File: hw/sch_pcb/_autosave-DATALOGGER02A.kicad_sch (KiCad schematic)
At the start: 9 parts

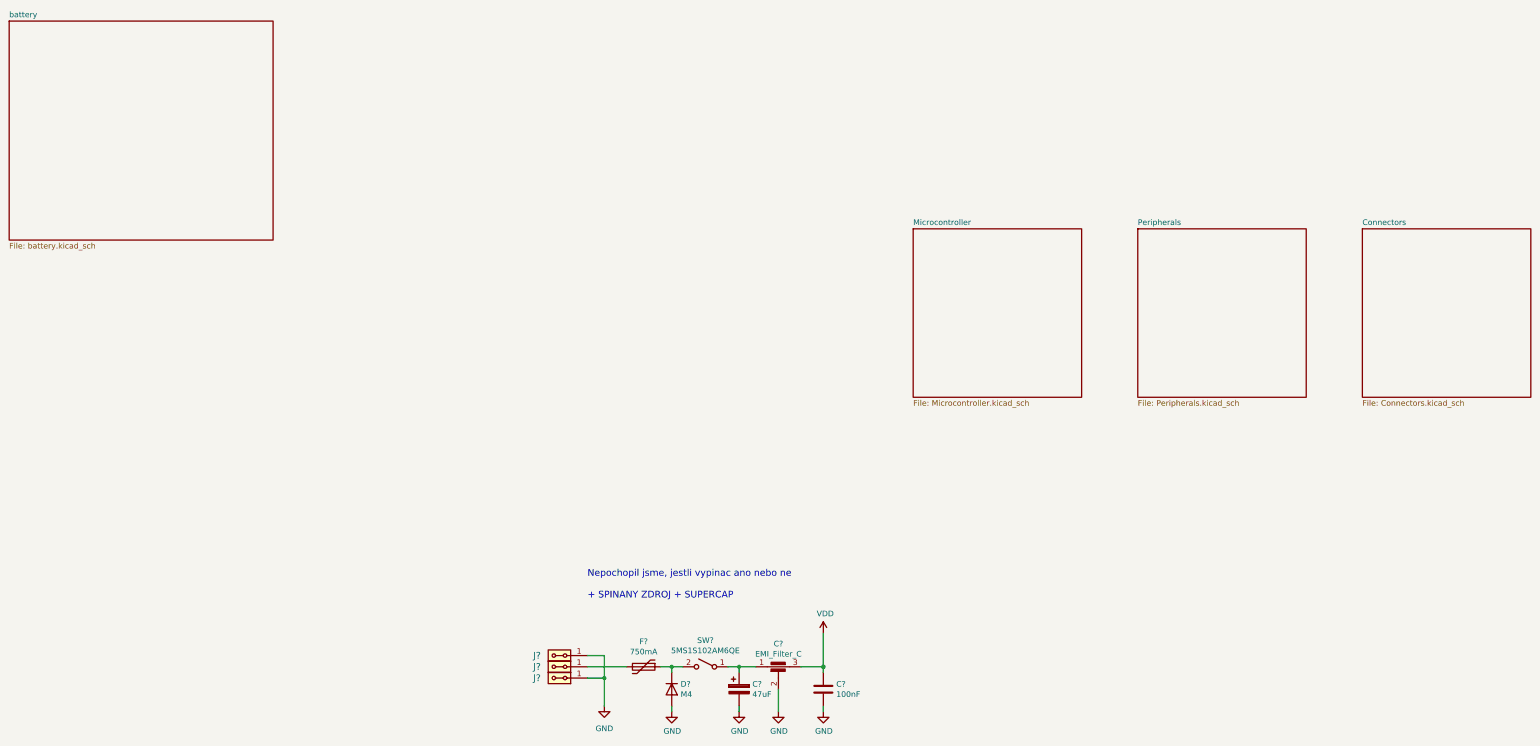
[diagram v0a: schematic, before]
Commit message: update of schematics
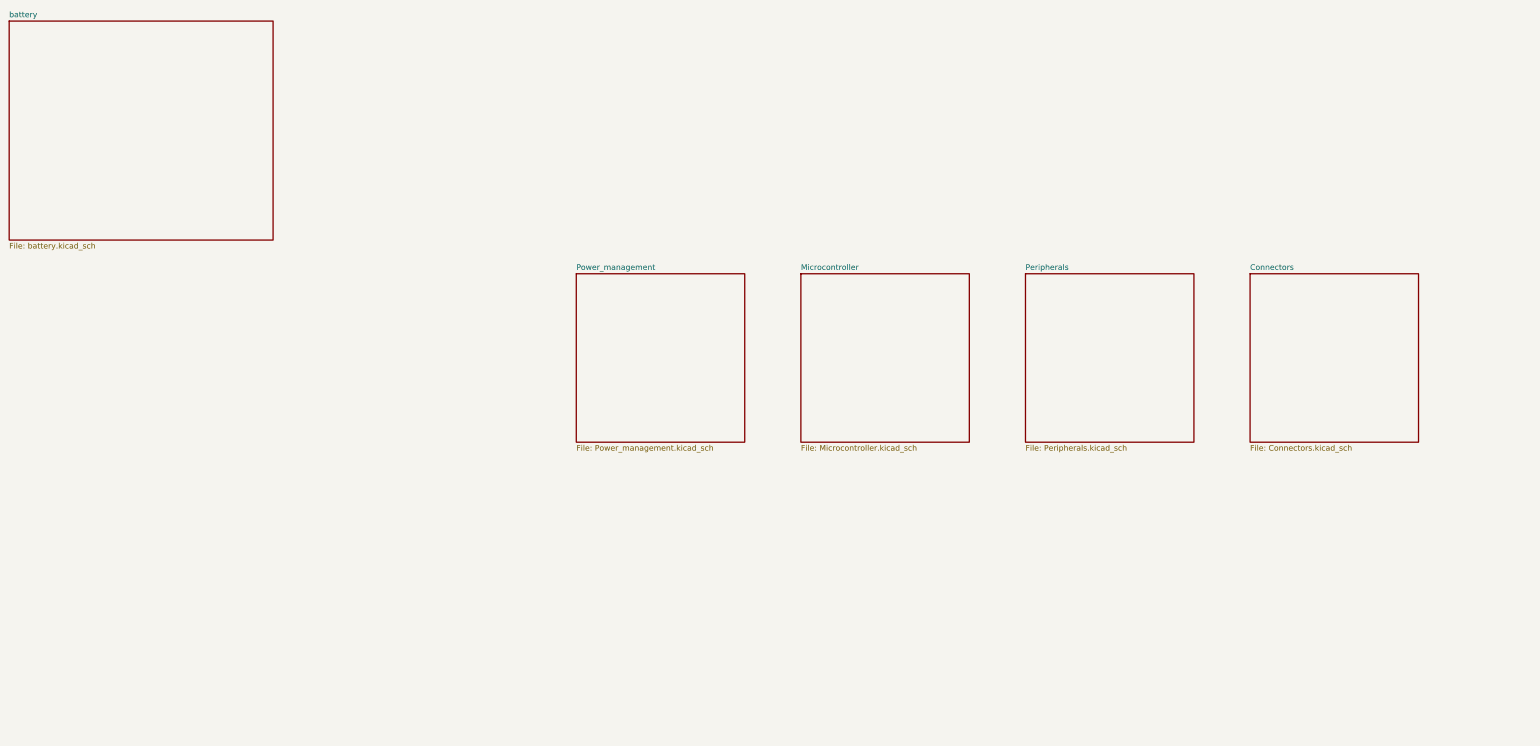
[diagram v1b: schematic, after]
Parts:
- removed C?: 47uF, Mlab_C:TantalC_SizeC_Reflow, symbol DATALOGGER01A-rescue:CP-device
- removed C?: 100nF, Mlab_R:SMD-0805, symbol DATALOGGER01A-rescue:C-device
- removed C?: EMI_Filter_C, Mlab_L:FIR1, symbol DATALOGGER01A-rescue:EMI_Filter_C-device
- removed D?: M4, Mlab_D:SMA_Standard, symbol DATALOGGER01A-rescue:D-device
- removed F?: 750mA, Mlab_F:1812, symbol DATALOGGER01A-rescue:Polyfuse-device
- removed J? (x3): HEADER_2x01_PARALLEL, Mlab_Pin_Headers:Straight_2x01, symbol DATALOGGER01A-rescue:HEADER_2x01_PARALLEL-MLAB_HEADER
- removed SW?: 5MS1S102AM6QE, Mlab_SW:5MS1S102AM6QE, symbol Switch:SW_SPST
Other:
- added sheet Power_management (Power_management.kicad_sch)
- note removed: "Nepochopil jsme, jestli vypinac ano nebo ne + SPINANY ZDROJ + SUPERCAP"
